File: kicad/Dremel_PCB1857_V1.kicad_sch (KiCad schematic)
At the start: 0 parts

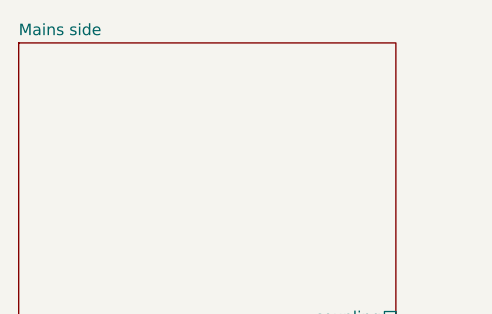
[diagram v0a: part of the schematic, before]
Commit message: Repair resonant circuitry
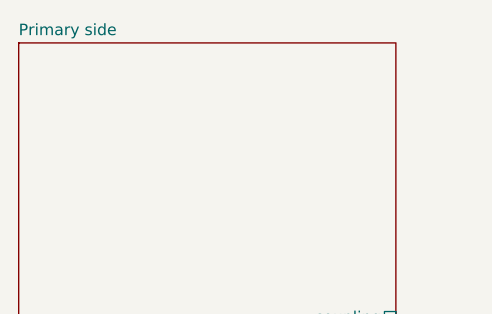
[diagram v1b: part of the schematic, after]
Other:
- sheet Mains side renamed Primary side
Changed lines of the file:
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@@
     (stroke (width 0.1524) (type solid))
     (fill (color 0 0 0 0.0000))
-    (property "Sheetname" "Mains side" (at 68.58 69.1384 0)
+    (property "Sheetname" "Primary side" (at 68.58 69.1384 0)
       (effects (font (size 1.27 1.27)) (justify left bottom))
     )

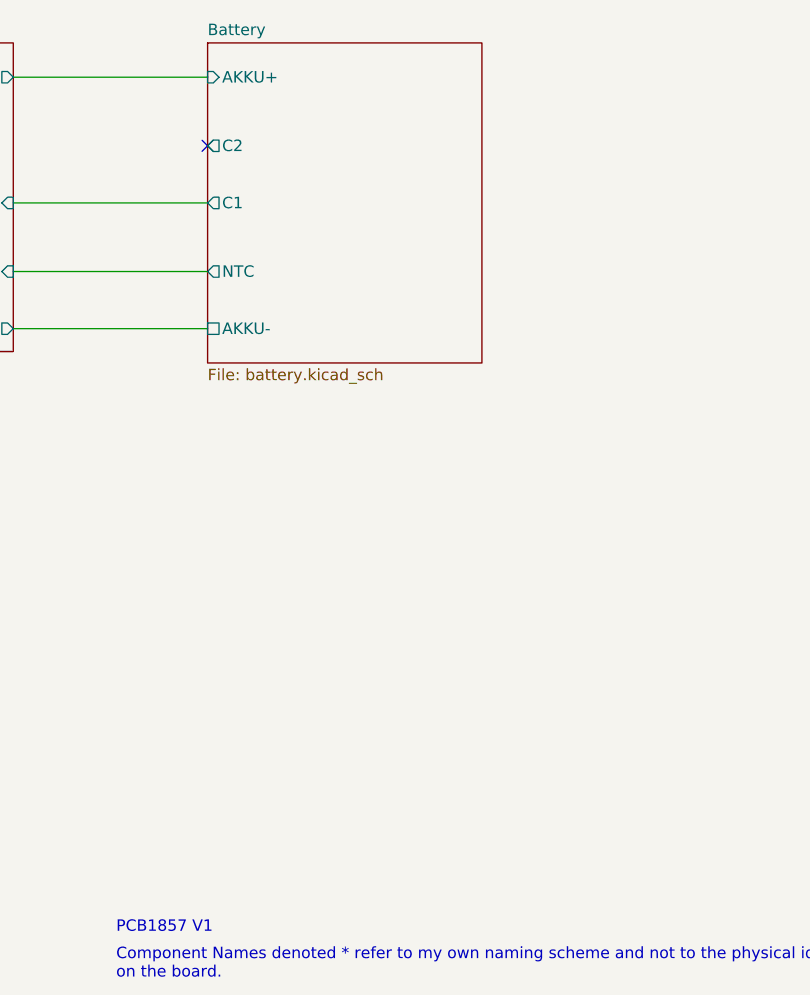
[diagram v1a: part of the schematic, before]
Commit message: Adds dremel battery schematic
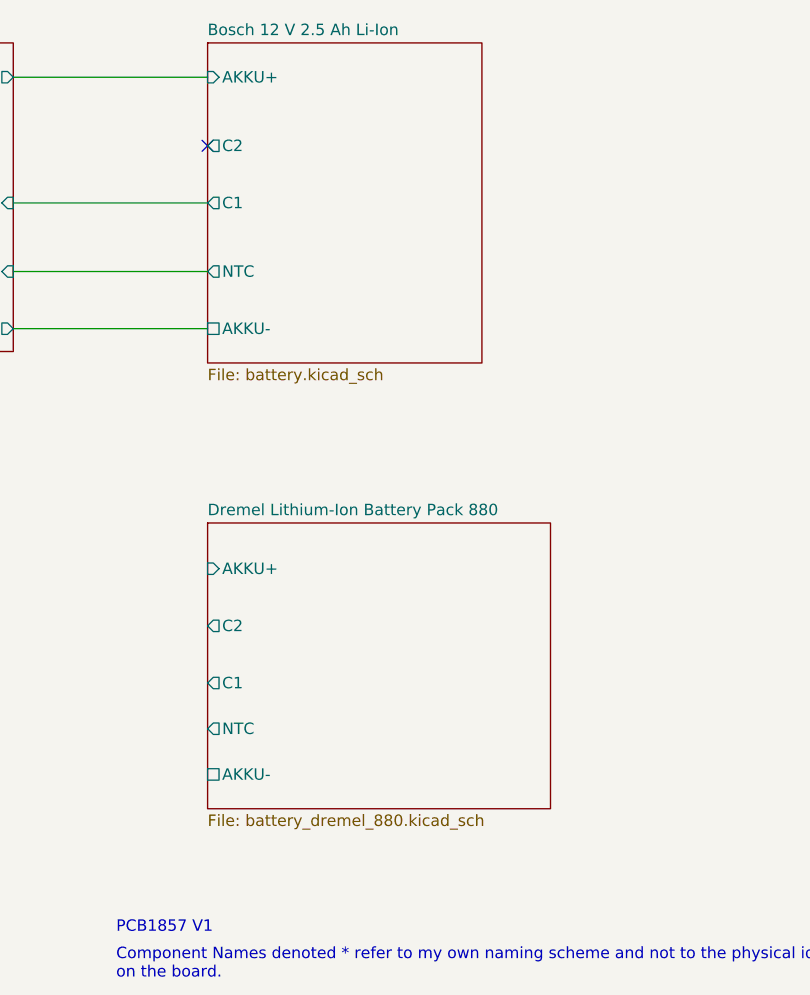
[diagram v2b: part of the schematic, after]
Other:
- sheet Battery renamed Bosch 12 V 2.5 Ah Li-Ion
- added sheet Dremel Lithium-Ion Battery Pack 880 (battery_dremel_880.kicad_sch)
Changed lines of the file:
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@@
     (effects (font (size 1.27 1.27)) (justify left bottom))
+  )
+  (sheet (at 187.96 123.19) (size 38.1 31.75) (fields_autoplaced)
+    (stroke (width 0.1524) (type solid))
+    (fill (color 0 0 0 0.0000))
+    (property "Sheetname" "Dremel Lithium-Ion Battery Pack 880" (at 187.96 122.4784 0)
+      (effects (font (size 1.27 1.27)) (justify left bottom))
+    )
+    (property "Sheetfile" "battery_dremel_880.kicad_sch" (at 187.96 155.5246 0)
+      (effects (font (size 1.27 1.27)) (justify left top))
+    )
+    (pin "AKKU-" passive (at 187.96 151.13 180)
+      (effects (font (size 1.27 1.27)) (justify left))
+    )
+    (pin "NTC" output (at 187.96 146.05 180)
+      (effects (font (size 1.27 1.27)) (justify left))
+    )
+    (pin "C2" output (at 187.96 134.62 180)
+      (effects (font (size 1.27 1.27)) (justify left))
+    )
+    (pin "C1" output (at 187.96 140.97 180)
+      (effects (font (size 1.27 1.27)) (justify left))
+    )
+    (pin "AKKU+" input (at 187.96 128.27 180)
+      (effects (font (size 1.27 1.27)) (justify left))
+    )
+    (instances
+      (project "Dremel_PCB1857_V1"
+        (path "/ab18b4c8-6f40-44db-bccd-b69c22b3ada9" (page "5"))
+      )
+    )
   )
   (sheet (at 68.58 69.85) (size 41.91 34.29) (fields_autoplaced)
@@
     (stroke (width 0.1524) (type solid))
     (fill (color 0 0 0 0.0000))
-    (property "Sheetname" "Battery" (at 187.96 69.1384 0)
+    (property "Sheetname" "Bosch 12 V 2.5 Ah Li-Ion" (at 187.96 69.1384 0)
       (effects (font (size 1.27 1.27)) (justify left bottom))
     )
